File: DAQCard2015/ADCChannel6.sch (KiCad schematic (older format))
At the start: 16 parts, among them U15 THS4524IDBTR, U16 AD9219

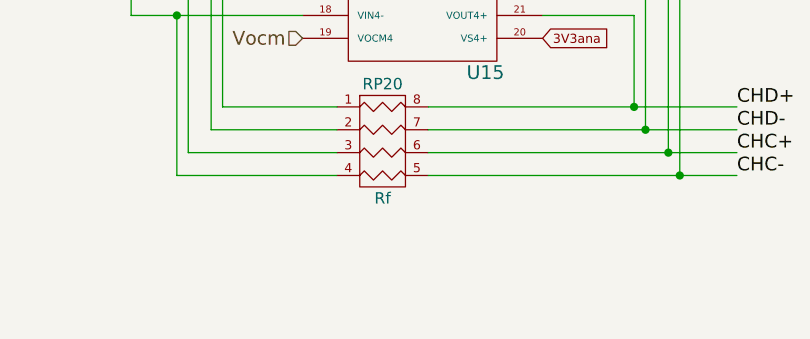
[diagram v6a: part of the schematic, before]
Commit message: Update to DAQ Board including adding an JTAG header and hooking up external clock and trigger
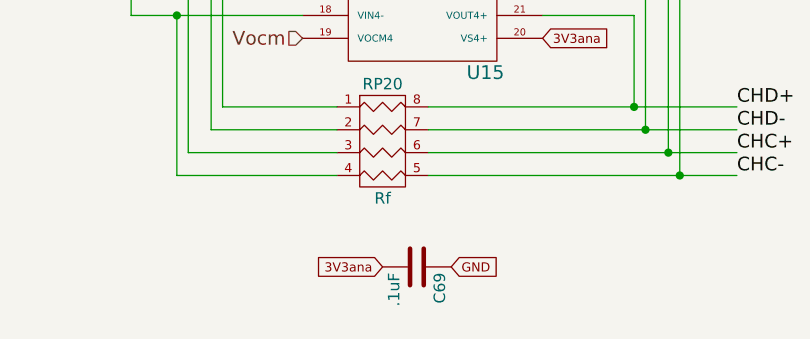
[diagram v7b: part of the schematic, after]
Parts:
- added C69: .1uF, Capacitors_SMD:C_0603, symbol C
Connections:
- net 3V3ana: now also C69.2
- net GND: now also C69.1
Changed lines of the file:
@@
 $Descr A4 11693 8268
 encoding utf-8
-Sheet 3 13
+Sheet 11 13
 Title ""
 Date ""
@@
 Text GLabel 8100 4150 0    40   Input ~ 0
 GND
+$Comp
+L C C69
+U 1 1 56064445
+P 4400 5500
+F 0 "C69" H 4425 5600 50  0000 L CNN
+F 1 ".1uF" H 4425 5400 50  0000 L CNN
+F 2 "Capacitors_SMD:C_0603" H 4438 5350 30  0001 C CNN
+F 3 "" H 4400 5500 60  0000 C CNN
+	1    4400 5500
+	0    1    1    0
+$EndComp
+Text GLabel 4250 5500 0    40   Input ~ 0
+3V3ana
+Text GLabel 4550 5500 2    40   Input ~ 0
+GND
 $EndSCHEMATC

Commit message: Adds digipart field to all parts that is now used in automatic generation of BOM(see DAQCard2015.html)
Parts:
- C41, C42, C43, C45, C46, C69: digipart (none) -> 445-1316-1-ND
- C44: digipart (none) -> 445-1420-1-ND
- R36, R37, R38, R39: digipart (none) -> P107HCT-ND
- R40: digipart (none) -> P10.0KHCT-ND
- RP19: digipart (none) -> RHM1564CT-ND
- RP20, RP21: digipart (none) -> RHM1336CT-ND
- U15: digipart (none) -> 296-24315-1-ND
- U16: digipart (none) -> AD9219ABCPZ-40-ND
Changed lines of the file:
@@
 F 2 "extras:QFN-48-1EP" H 8650 3700 60  0001 C CNN
 F 3 "" H 8650 3700 60  0000 C CNN
+F 4 "AD9219ABCPZ-40-ND" H 9050 3700 60  0001 C CNN "digipart"
 	1    9050 3700
 	1    0    0    -1
@@
 F 2 "Capacitors_SMD:C_0603" H 7588 3500 30  0001 C CNN
 F 3 "" H 7550 3650 60  0000 C CNN
+F 4 "445-1316-1-ND" H 7550 3650 60  0001 C CNN "digipart"
 	1    7550 3650
 	0    1    1    0
@@
 F 2 "Capacitors_SMD:C_0603" H 7588 3800 30  0001 C CNN
 F 3 "" H 7550 3950 60  0000 C CNN
+F 4 "445-1316-1-ND" H 7550 3950 60  0001 C CNN "digipart"
 	1    7550 3950
 	0    1    1    0
@@
 F 2 "Capacitors_SMD:C_0603" H 9338 1600 30  0001 C CNN
 F 3 "" H 9300 1750 60  0000 C CNN
+F 4 "445-1316-1-ND" H 9300 1750 60  0001 C CNN "digipart"
 	1    9300 1750
 	0    1    1    0
@@
 F 2 "Capacitors_SMD:C_0603" H 8638 1600 30  0001 C CNN
 F 3 "" H 8600 1750 60  0000 C CNN
+F 4 "445-1316-1-ND" H 8600 1750 60  0001 C CNN "digipart"
 	1    8600 1750
 	0    1    1    0
@@
 F 2 "Capacitors_SMD:C_0603" H 8988 1500 30  0001 C CNN
 F 3 "" H 8950 1650 60  0000 C CNN
+F 4 "445-1316-1-ND" H 8950 1650 60  0001 C CNN "digipart"
 	1    8950 1650
 	0    1    1    0
@@
 F 2 "Resistors_SMD:R_0603" V 9830 1950 30  0001 C CNN
 F 3 "" H 9900 1950 30  0000 C CNN
+F 4 "P10.0KHCT-ND" V 9900 1950 60  0001 C CNN "digipart"
 	1    9900 1950
 	0    1    1    0
@@
 F 2 "extras:TSSOP-38_4.4x9.7mm_Pitch0.5mm" H 4600 3800 60  0001 C CNN
 F 3 "" H 4600 3800 60  0000 C CNN
+F 4 "296-24315-1-ND" H 4400 3700 60  0001 C CNN "digipart"
 	1    4400 3700
 	1    0    0    -1
@@
 F 2 "Resistors_SMD:R_0603" V 1780 4350 30  0001 C CNN
 F 3 "" H 1850 4350 30  0000 C CNN
+F 4 "P107HCT-ND" V 1850 4350 60  0001 C CNN "digipart"
 	1    1850 4350
 	1    0    0    -1
@@
 F 2 "Resistors_SMD:R_0603" V 1780 3850 30  0001 C CNN
 F 3 "" H 1850 3850 30  0000 C CNN
+F 4 "P107HCT-ND" V 1850 3850 60  0001 C CNN "digipart"
 	1    1850 3850
 	1    0    0    -1
@@
 F 2 "Resistors_SMD:R_0603" V 1780 3350 30  0001 C CNN
 F 3 "" H 1850 3350 30  0000 C CNN
+F 4 "P107HCT-ND" V 1850 3350 60  0001 C CNN "digipart"
 	1    1850 3350
 	1    0    0    -1
@@
 F 2 "Resistors_SMD:R_0603" V 1780 2850 30  0001 C CNN
 F 3 "" H 1850 2850 30  0000 C CNN
+F 4 "P107HCT-ND" V 1850 2850 60  0001 C CNN "digipart"
 	1    1850 2850
 	1    0    0    -1
@@
 F 2 "extras:R4-MNR04" H 4250 5150 60  0001 C CNN
 F 3 "" H 4250 5150 60  0000 C CNN
+F 4 "RHM1336CT-ND" H 4250 5150 60  0001 C CNN "digipart"
 	1    4250 5150
 	1    0    0    -1
@@
 F 2 "extras:R4-MNR04" H 4300 2450 60  0001 C CNN
 F 3 "" H 4300 2450 60  0000 C CNN
+F 4 "RHM1336CT-ND" H 4300 2450 60  0001 C CNN "digipart"
 	1    4300 2450
 	1    0    0    -1
@@
 F 2 "extras:R8_MNR18" H 2750 3600 60  0001 C CNN
 F 3 "" H 2750 3600 60  0000 C CNN
+F 4 "RHM1564CT-ND" H 2750 3600 60  0001 C CNN "digipart"
 	1    2750 3600
 	1    0    0    -1
@@
 F 2 "Capacitors_SMD:C_0805" H 8988 1300 30  0001 C CNN
 F 3 "" H 8950 1450 60  0000 C CNN
+F 4 "445-1420-1-ND" H 8950 1450 60  0001 C CNN "digipart"
 	1    8950 1450
 	0    -1   -1   0
@@
 F 2 "Capacitors_SMD:C_0603" H 4438 5350 30  0001 C CNN
 F 3 "" H 4400 5500 60  0000 C CNN
+F 4 "445-1316-1-ND" H 4400 5500 60  0001 C CNN "digipart"
 	1    4400 5500
 	0    1    1    0
